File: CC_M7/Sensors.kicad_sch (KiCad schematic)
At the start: 12 parts, among them U11 IIM-42652, U2 BMI088, U4 BMM150, U5 24AA64T-I/OT

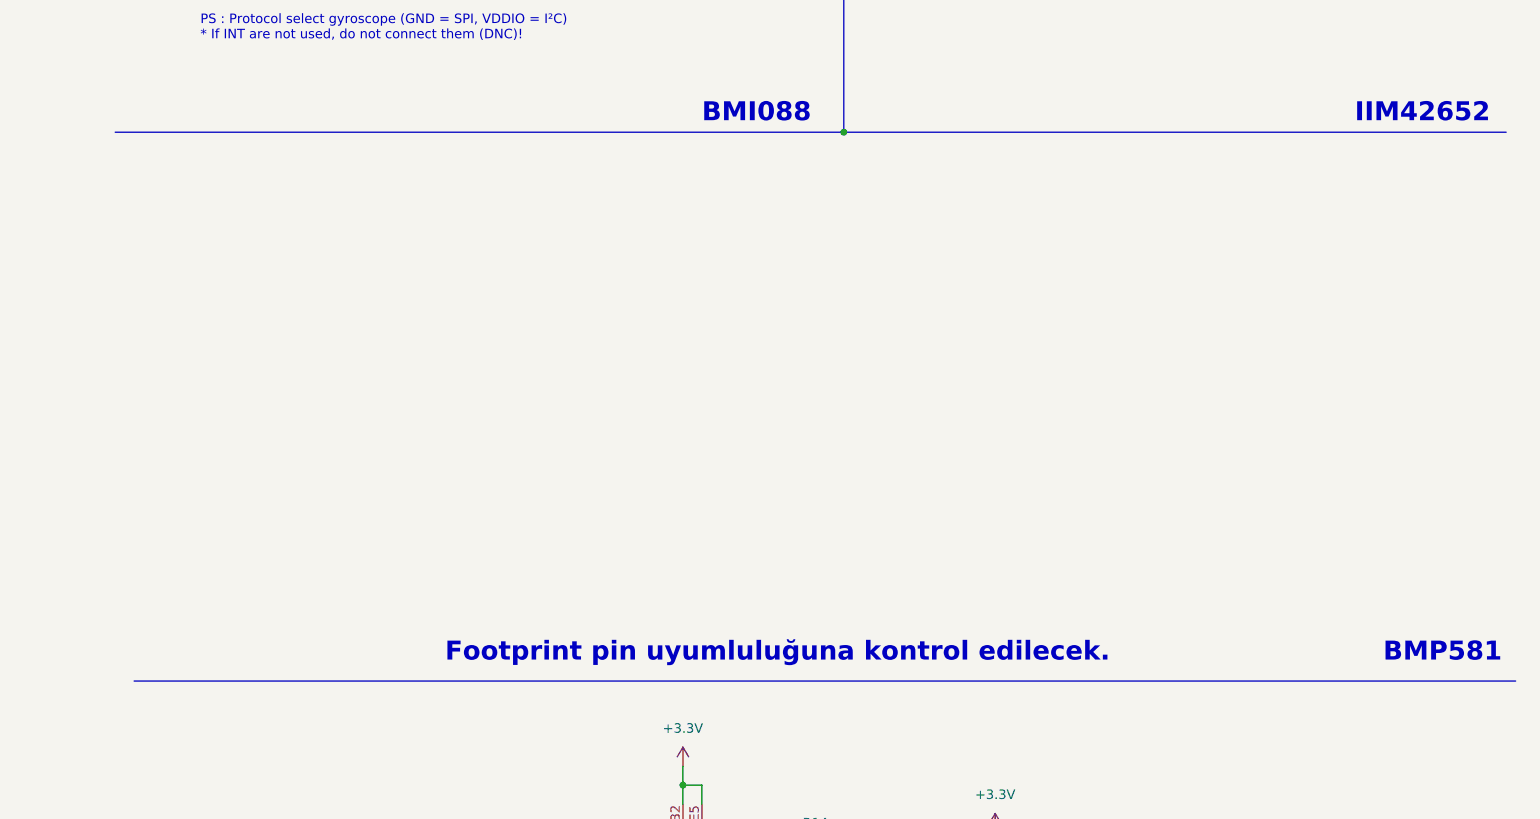
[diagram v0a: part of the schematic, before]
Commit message: BMP581 and ICP20100 added
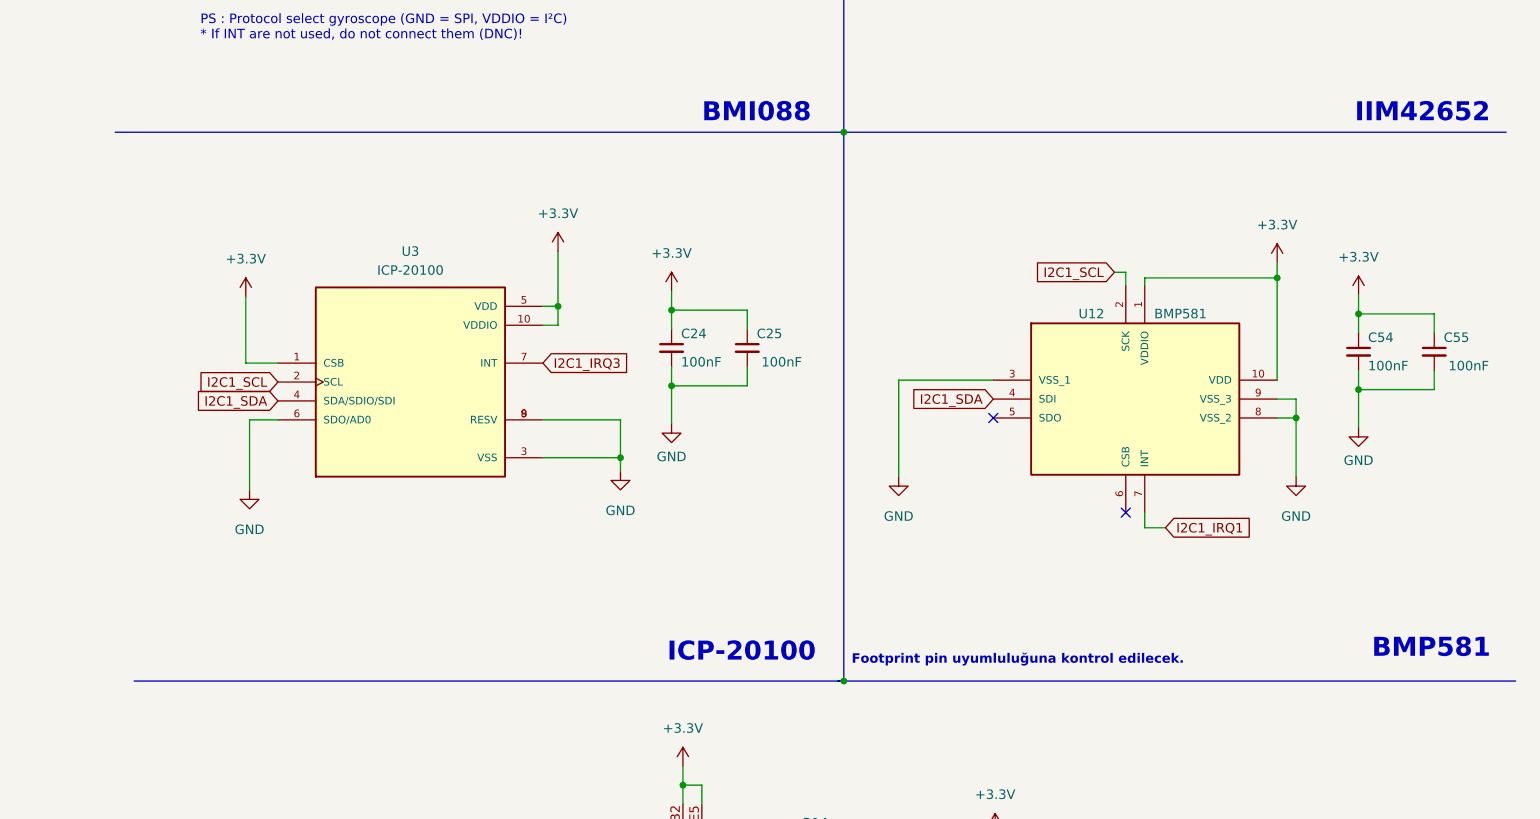
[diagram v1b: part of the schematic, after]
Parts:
- added C24, C25, C54, C55: 100nF, Capacitor_SMD:C_0603_1608Metric, symbol Device:C_Small
- added U12: BMP581, BMP581:BMP581, symbol BMP581:BMP581
- added U3: ICP-20100, ICP-20100:PQFN50P200X200X85-10N, symbol ICP-20100:ICP-20100
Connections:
- net +3.3V: now also C24.1, C25.1, C54.1, C55.1, U12.1 (VDDIO), U12.10 (VDD), U3.1 (CSB), U3.10 (VDDIO), U3.5 (VDD)
- net GND: now also C24.2, C25.2, C54.2, C55.2, U12.3 (VSS_1), U12.8 (VSS_2), U12.9 (VSS_3), U3.3 (VSS), U3.6 (SDO/AD0), U3.8 (RESV), U3.9 (RESV)
- net I2C1_SCL: now also U12.2 (SCK), U3.2 (SCL)
- net I2C1_SDA: now also U12.4 (SDI), U3.4 (SDA/SDIO/SDI)
- new net I2C1_IRQ1: U12.7 (INT)
- new net I2C1_IRQ3: U3.7 (INT)
- no-connect marks 7 -> 9
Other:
- note added: "ICP-20100"

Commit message: ready to start PCB drawing
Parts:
- removed R14: 1k, Resistor_SMD:R_0805_2012Metric, symbol Device:R_Small
- removed U11: IIM-42652, Package_LGA:Bosch_LGA-14_3x2.5mm_P0.5mm, symbol Sensor_Motion:IIM-42652
- removed U12: BMP581, BMP581:BMP581, symbol BMP581:BMP581
- removed U2: BMI088, BMI088:PQFN50P450X300X100-16N, symbol BMI088:BMI088
- removed U3: ICP-20100, ICP-20100:PQFN50P200X200X85-10N, symbol ICP-20100:ICP-20100
- removed U4: BMM150, Package_CSP:WLCSP-12_1.56x1.56mm_P0.4mm, symbol Sensor_Magnetic:BMM150
- removed U5: 24AA64T-I/OT, Package_TO_SOT_SMD:SOT-23-5_HandSoldering, symbol 2024-04-16_22-30-30:24AA64T-I_OT
- added R11: 1k, Resistor_SMD:R_0805_2012Metric, symbol Device:R_Small
- added U11: BMP581, BMP581:BMP581, symbol BMP581:BMP581
- added U12: IIM-42652, Package_LGA:Bosch_LGA-14_3x2.5mm_P0.5mm, symbol Sensor_Motion:IIM-42652
- added U2: 24AA64T-I/OT, Package_TO_SOT_SMD:SOT-23-5_HandSoldering, symbol 2024-04-16_22-30-30:24AA64T-I_OT
- added U3: BMI088, BMI088:PQFN50P450X300X100-16N, symbol BMI088:BMI088
- added U4: ICP-20100, ICP-20100:PQFN50P200X200X85-10N, symbol ICP-20100:ICP-20100
- added U5: BMM150, Package_CSP:WLCSP-12_1.56x1.56mm_P0.4mm, symbol Sensor_Magnetic:BMM150
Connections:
- net +3.3V: now also U11.1 (VDDIO), U11.10 (VDD), U12.5 (VDDIO), U12.8 (VDD), U2.4 (VCC), U3.11 (VDDIO), U3.3 (VDD), U4.1 (CSB), U4.10 (VDDIO), U4.5 (VDD), U5.A1 (PS), U5.B2 (VDDIO), U5.E5 (VDD)
- net GND: now also U11.3 (VSS_1), U11.8 (VSS_2), U11.9 (VSS_3), U12.6 (GND), U12.7 (GND), U2.2 (VSS), U2.5 (WP), U3.2 (NC), U3.4 (GNDA), U3.6 (GNDIO), U3.7 (PS), U4.3 (VSS), U4.6 (SDO/AD0), U4.8 (RESV), U4.9 (RESV), U5.A5 (CSB), U5.C1 (SDO), U5.C5 (GND), U5.E1 (GND), U5.E3 (GND)
- net I2C1_IRQ1: now also U11.7 (INT)
- net I2C1_IRQ2: now also R11.2
- net I2C1_IRQ3: now also U4.7 (INT)
- net I2C1_SCL: now also U11.2 (SCK), U2.1 (SCL), U4.2 (SCL), U5.A3 (SCK)
- net I2C1_SDA: now also U11.4 (SDI), U2.3 (SDA), U4.4 (SDA/SDIO/SDI), U5.B4 (SDI)
- net SPI1_CS1: now also U3.14 (CSB1)
- net SPI1_CS2: now also U3.5 (CSB2)
- net SPI1_CS3: now also U12.12 (AP_CS)
- net SPI1_MISO: now also U12.1 (AP_SDO/AP_AD0), U3.10 (SDO2), U3.15 (SDO1)
- net SPI1_MOSI: now also U12.14 (AP_SDA/AP_SDIO/AP_SDI), U3.9 (SDA/SDI)
- net SPI1_SCK: now also U3.8 (SCL/SCK)
- new net: R11.1, U5.D4 (DRDY)
- no-connect marks 9 -> 10
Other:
- note added: "I2C Adresses AD0 = 0 0x63 AD0 = 1 0x64"
- note removed: "I2C adresleri yazılacak"

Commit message: nRF PCB placement completed
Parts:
- R11: footprint Resistor_SMD:R_0805_2012Metric -> Resistor_SMD:R_0603_1608Metric
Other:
- note added: "FOOTPRINT WILL BE CHANGED!!!!!"
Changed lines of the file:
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@@
+		)
+	)
+	(text "FOOTPRINT WILL BE CHANGED!!!!!"
+		(exclude_from_sim no)
+		(at 152.4 177.8 0)
+		(effects
+			(font
+				(size 2.54 2.54)
+				(thickness 0.508)
+				(bold yes)
+			)
 		)
 	)
@@
 			)
 		)
-		(property "Footprint" "Resistor_SMD:R_0805_2012Metric"
+		(property "Footprint" "Resistor_SMD:R_0603_1608Metric"
 			(at 104.14 191.77 0)
 			(effects

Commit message: Component placement completed
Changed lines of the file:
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@@
 	(global_label "I2C1_IRQ1"
 		(shape input)
-		(at 148.59 143.51 0)
+		(at 148.59 143.51 270)
 		(fields_autoplaced yes)
 		(effects
@@
 				(size 1.27 1.27)
 			)
-			(justify left)
+			(justify right)
 		)
 		(property "Intersheetrefs" "${INTERSHEET_REFS}"
-			(at 161.2514 143.51 0)
+			(at 148.59 156.1714 90)
 			(effects
 				(font
 					(size 1.27 1.27)
 				)
-				(justify left)
+				(justify right)
 				(hide yes)
 			)

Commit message: Reverse current protection added. | Routing progress.
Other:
- note removed: "FOOTPRINT WILL BE CHANGED!!!!!"
- moved on the sheet: C22, C24, U3

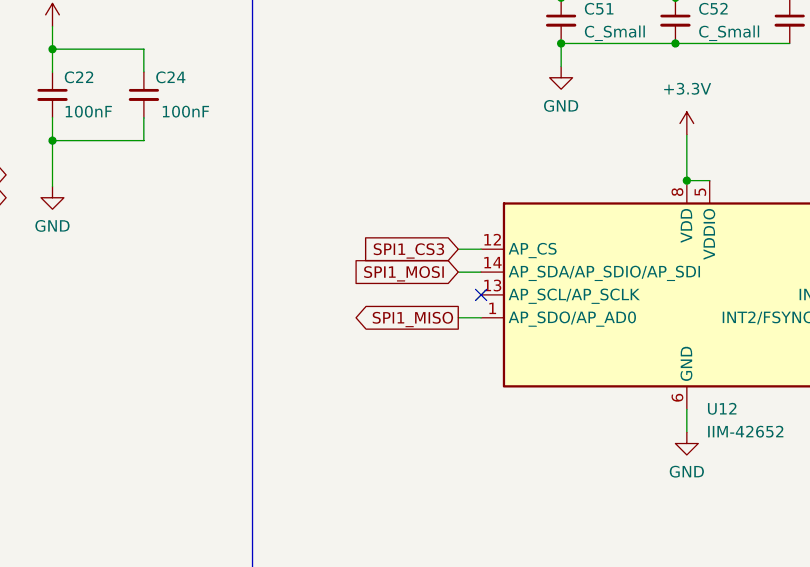
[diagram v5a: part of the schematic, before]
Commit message: Routing Progress | BMM150 removed.
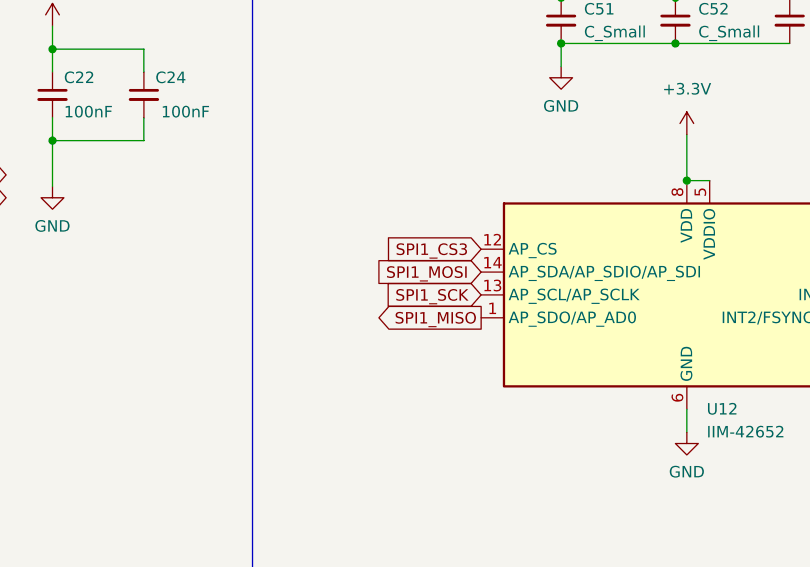
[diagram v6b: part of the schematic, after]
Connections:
- net SPI1_SCK: now also U12.13 (AP_SCL/AP_SCLK)
- no-connect marks 10 -> 9
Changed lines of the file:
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@@
-	)
-	(no_connect
-		(at 133.35 55.88)
 	)
 	(no_connect
@@
 	(wire
 		(pts
-			(xy 130.81 50.8) (xy 133.35 50.8)
-		)
-		(stroke
-			(width 0)
-			(type default)
-		)
-	)
-	(wire
-		(pts
 			(xy 85.09 129.54) (xy 85.09 132.08)
 		)
@@
 	(wire
 		(pts
-			(xy 130.81 58.42) (xy 133.35 58.42)
-		)
-		(stroke
-			(width 0)
-			(type default)
-		)
-	)
-	(wire
-		(pts
 			(xy 95.25 124.46) (xy 95.25 121.92)
 		)
@@
 		(pts
 			(xy 74.93 262.89) (xy 69.85 262.89)
-		)
-		(stroke
-			(width 0)
-			(type default)
-		)
-	)
-	(wire
-		(pts
-			(xy 130.81 53.34) (xy 133.35 53.34)
 		)
 		(stroke
@@
 	(global_label "SPI1_MISO"
 		(shape output)
-		(at 130.81 58.42 180)
+		(at 133.35 58.42 180)
 		(fields_autoplaced yes)
 		(effects
@@
 		)
 		(property "Intersheetrefs" "${INTERSHEET_REFS}"
-			(at 117.9672 58.42 0)
+			(at 120.5072 58.42 0)
 			(effects
 				(font
@@
 	(global_label "SPI1_MOSI"
 		(shape input)
-		(at 130.81 53.34 180)
+		(at 133.35 53.34 180)
 		(fields_autoplaced yes)
 		(effects
@@
 		)
 		(property "Intersheetrefs" "${INTERSHEET_REFS}"
-			(at 117.9672 53.34 0)
+			(at 120.5072 53.34 0)
 			(effects
 				(font
@@
 	(global_label "SPI1_CS3"
 		(shape input)
-		(at 130.81 50.8 180)
+		(at 133.35 50.8 180)
 		(fields_autoplaced yes)
 		(effects
@@
 		)
 		(property "Intersheetrefs" "${INTERSHEET_REFS}"
-			(at 118.8744 50.8 0)
+			(at 121.4144 50.8 0)
 			(effects
 				(font
@@
 				(hide yes)
 			)
+		)
+	)
+	(global_label "SPI1_SCK"
+		(shape input)
+		(at 133.35 55.88 180)
+		(fields_autoplaced yes)
+		(effects
+			(font
+				(size 1.27 1.27)
+			)
+			(justify right)
+		)
+		(property "Intersheetrefs" "${INTERSHEET_REFS}"
+			(at 121.3539 55.88 0)
+			(effects
+				(font
+					(size 1.27 1.27)
+				)
+				(justify right)
+				(hide yes)
+			)
